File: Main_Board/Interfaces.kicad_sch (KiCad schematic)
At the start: 17 parts, among them J4 External bords interfaces, Q2 2N7002

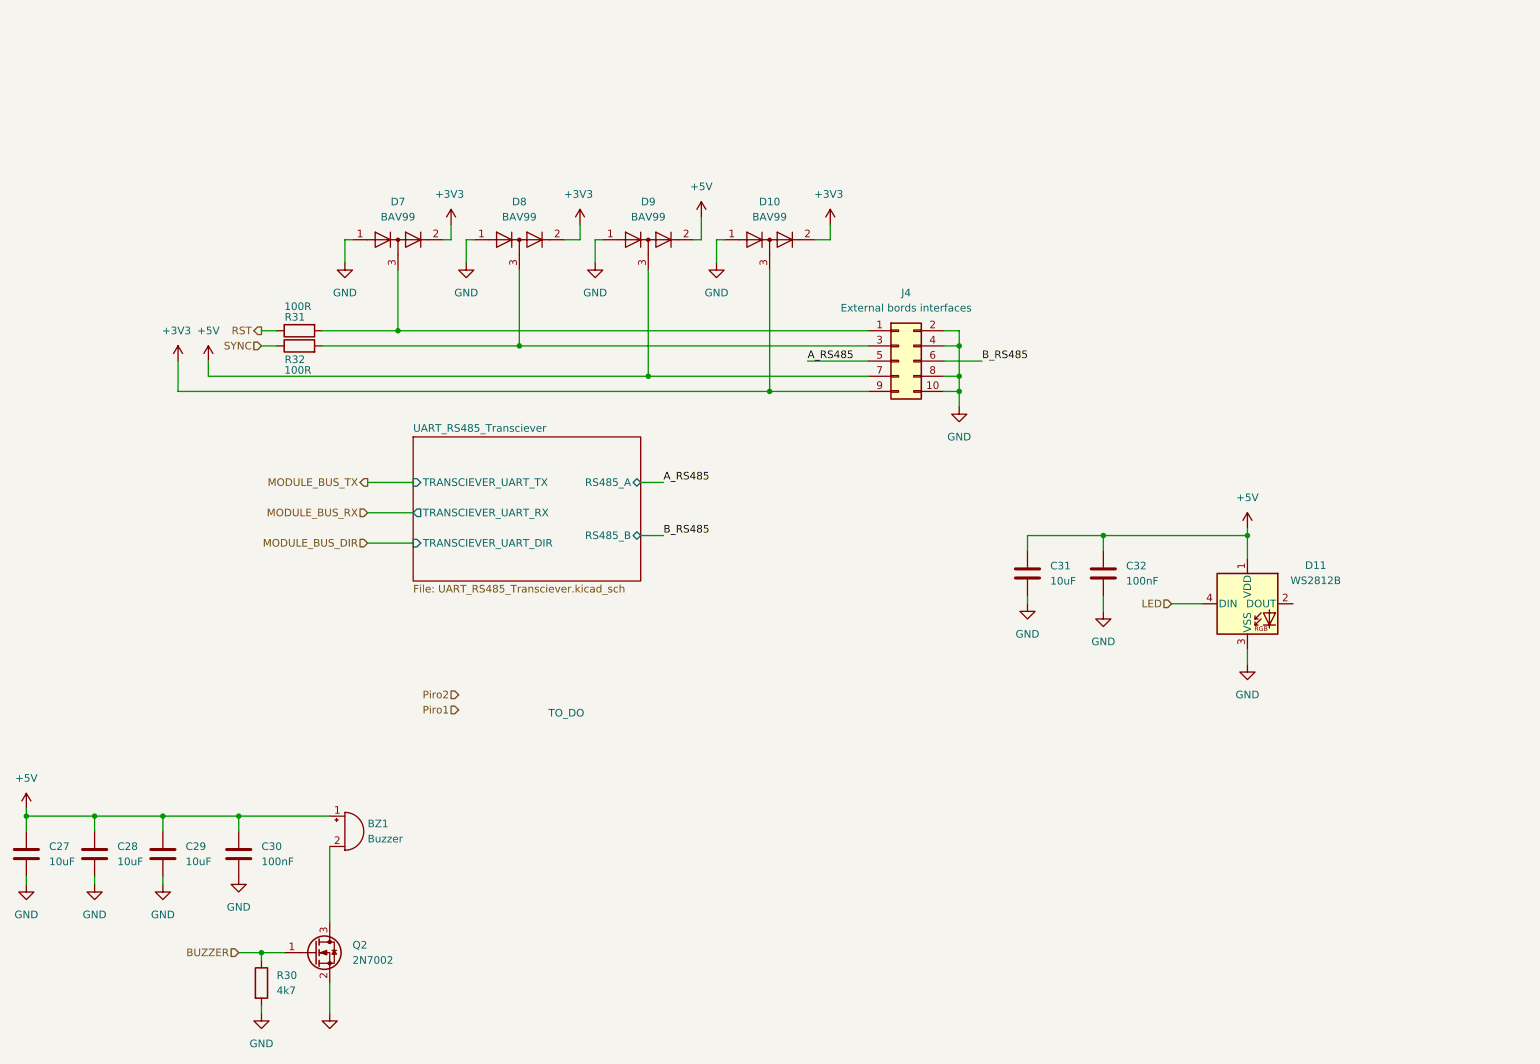
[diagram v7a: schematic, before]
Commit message: Module bus fix
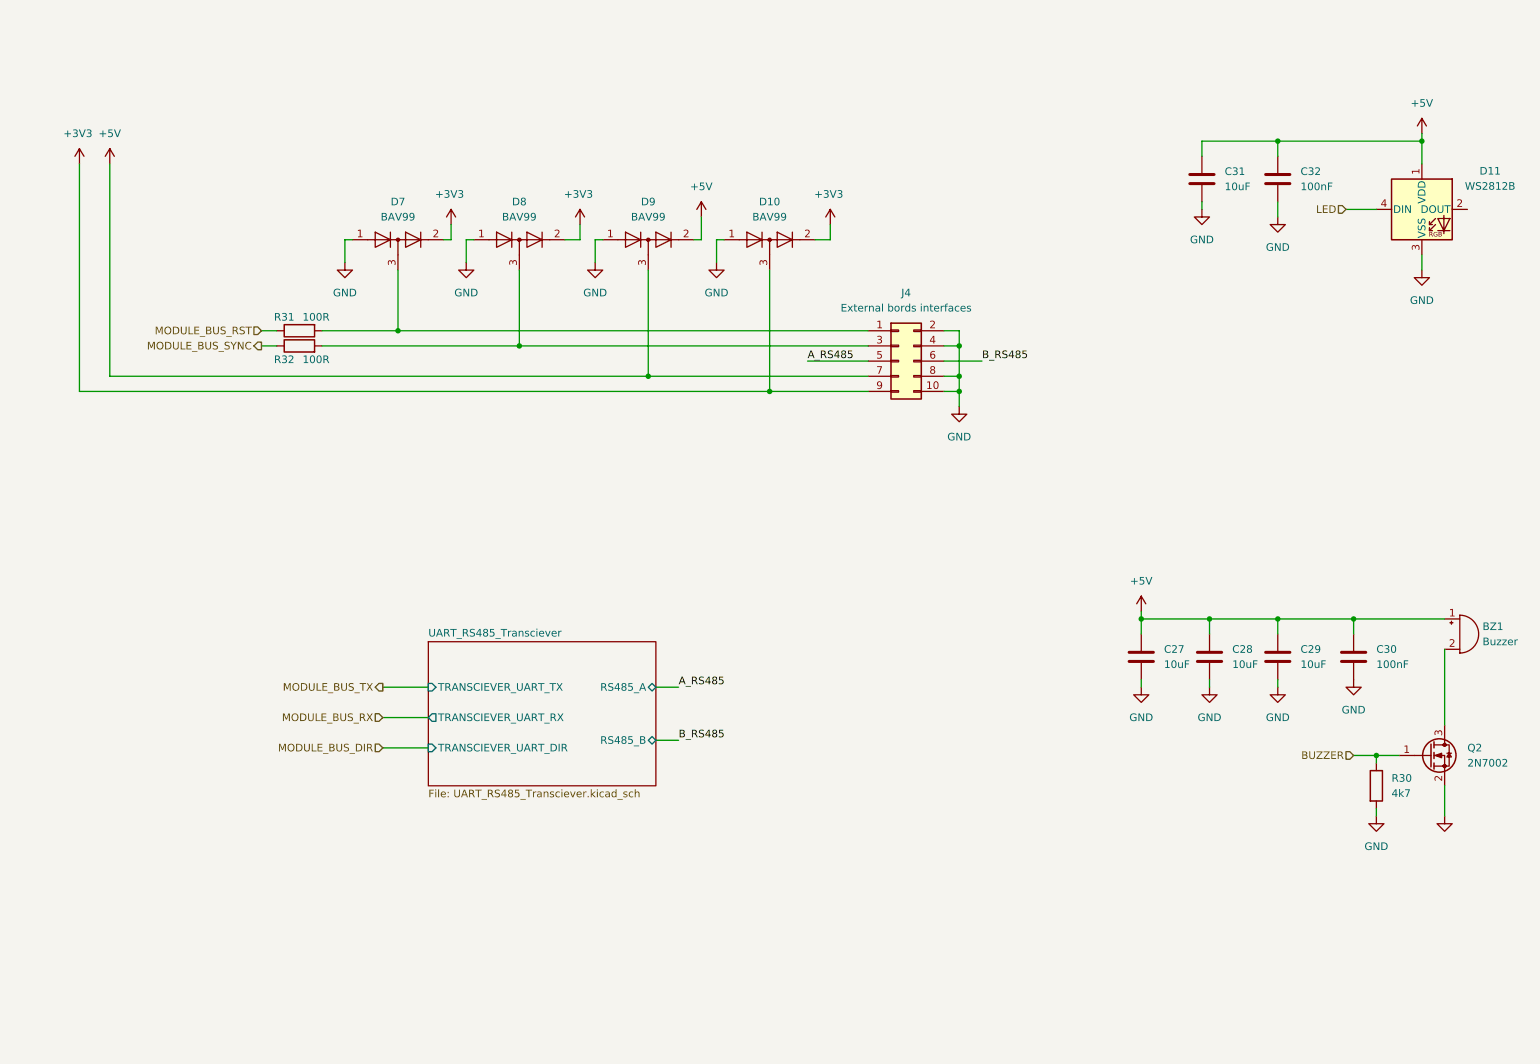
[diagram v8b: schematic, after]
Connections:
- net RST renamed MODULE_BUS_RST
- net SYNC renamed MODULE_BUS_SYNC
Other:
- note removed: "TO_DO"
- moved on the sheet: BZ1, C27, C28, C29, C30, C31, C32, D11, Q2, R30
